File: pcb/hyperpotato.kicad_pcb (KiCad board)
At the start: 2 copper layers, 116.5 x 93.7 mm, 37 parts, among them J1 Conn_01x02_Socket, J2 Conn_01x03_Pin, Q1 AO3401A, SW1 SW_Push_45deg, SW10 SW_Push_45deg, SW11 SW_Push_45deg, SW12 SW_Push_45deg, SW13 SW_Push_45deg, SW14 SW_SPDT, SW15 SW_Push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

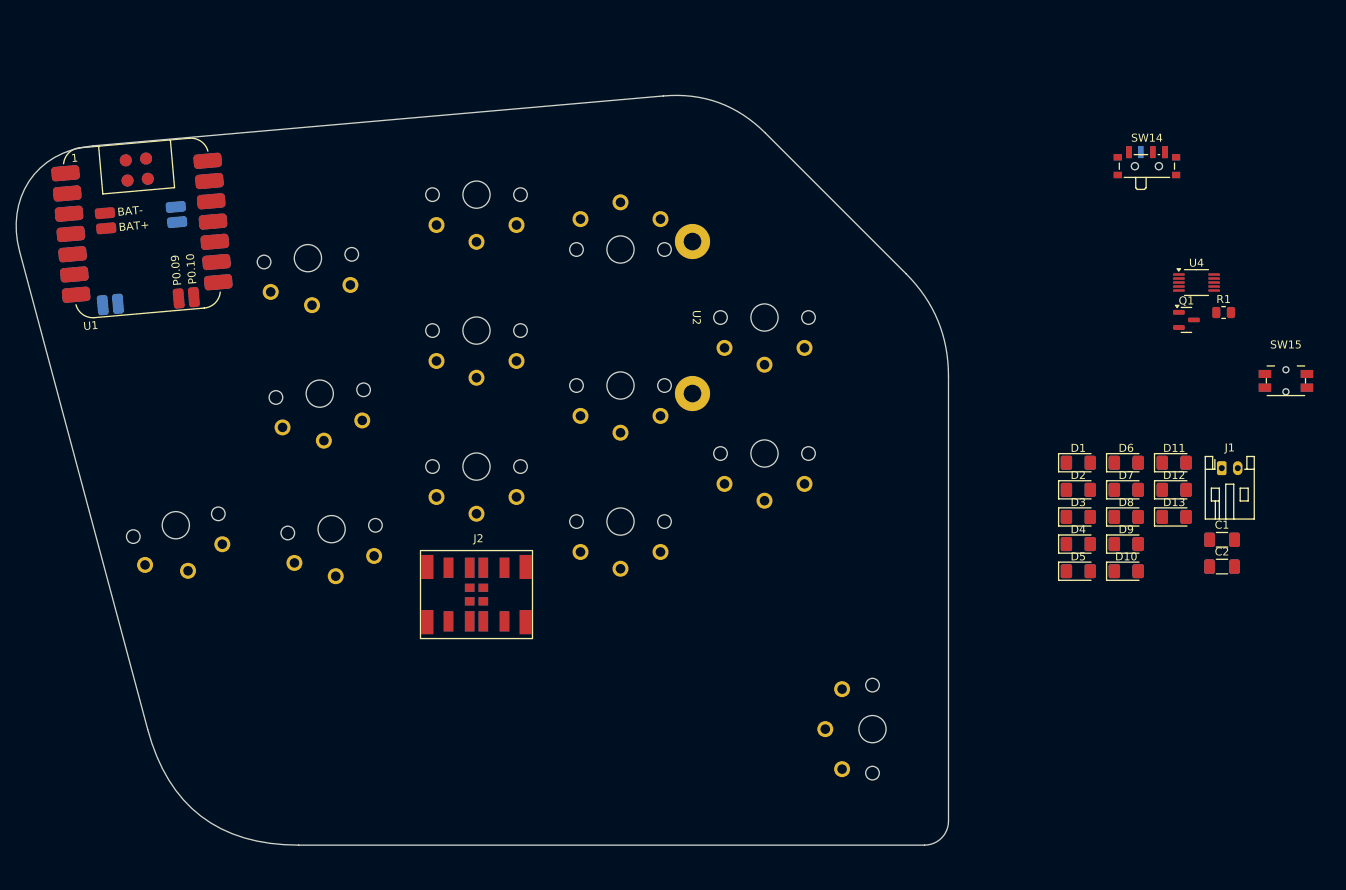
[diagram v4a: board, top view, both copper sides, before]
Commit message: Place diodes
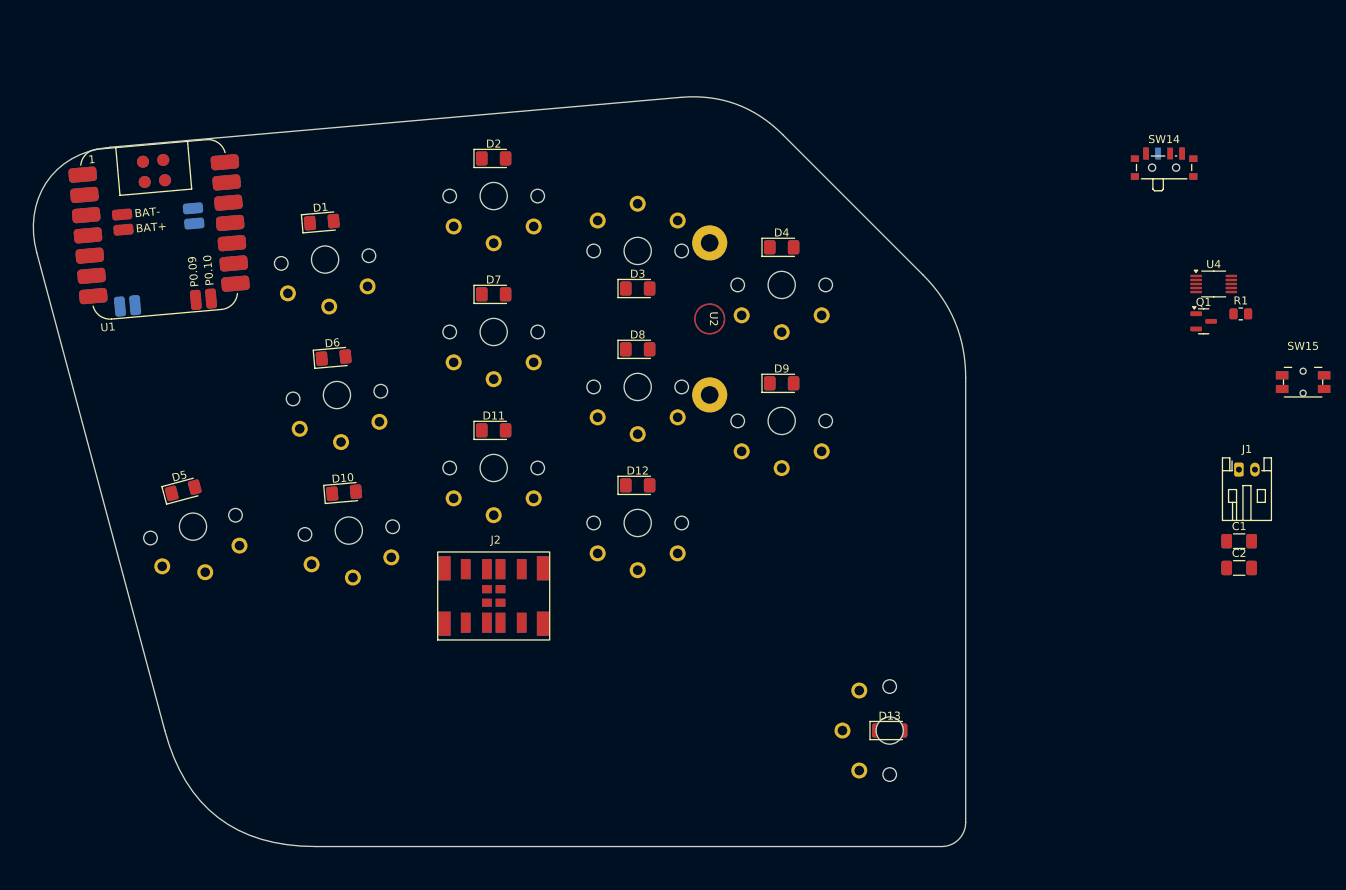
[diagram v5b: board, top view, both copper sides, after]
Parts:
- moved D5 112.3 mm to (59.0, 102.2), turned to 15 degrees
- moved D6 99.9 mm to (77.8, 85.6), turned to 5 degrees
- moved D1 99.2 mm to (76.3, 68.7), turned to 5 degrees
- moved D10 98.3 mm to (79.1, 102.5), turned to 5 degrees
- moved D11 85.2 mm to (97.8, 94.7)
- moved D2 84.0 mm to (97.8, 60.7)
- moved D7 82.8 mm to (97.8, 77.7)
- moved D12 67.1 mm to (115.8, 101.6)
- moved D8 64.6 mm to (115.8, 84.6)
- moved D3 62.0 mm to (115.8, 77.0)
- moved D4 52.4 mm to (133.8, 71.8)
- moved D9 47.5 mm to (133.8, 88.8)
- moved D13 44.5 mm to (147.3, 132.2)
- moved SW9 4.61 mm to (133.8, 93.5)
- moved SW4 4.61 mm to (133.8, 76.5)
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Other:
- board text added: "Trackpoint is going to be mounted on the right side, and the switch pin won't collide with it in this orientation. Will need to cut stab pins though."
- board text removed: "Trackpoint is going to be mounted on the right side, and the switch pin won't collide with it in this orientation. Will need to cut stab pin though."

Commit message: Re-arrange diodes
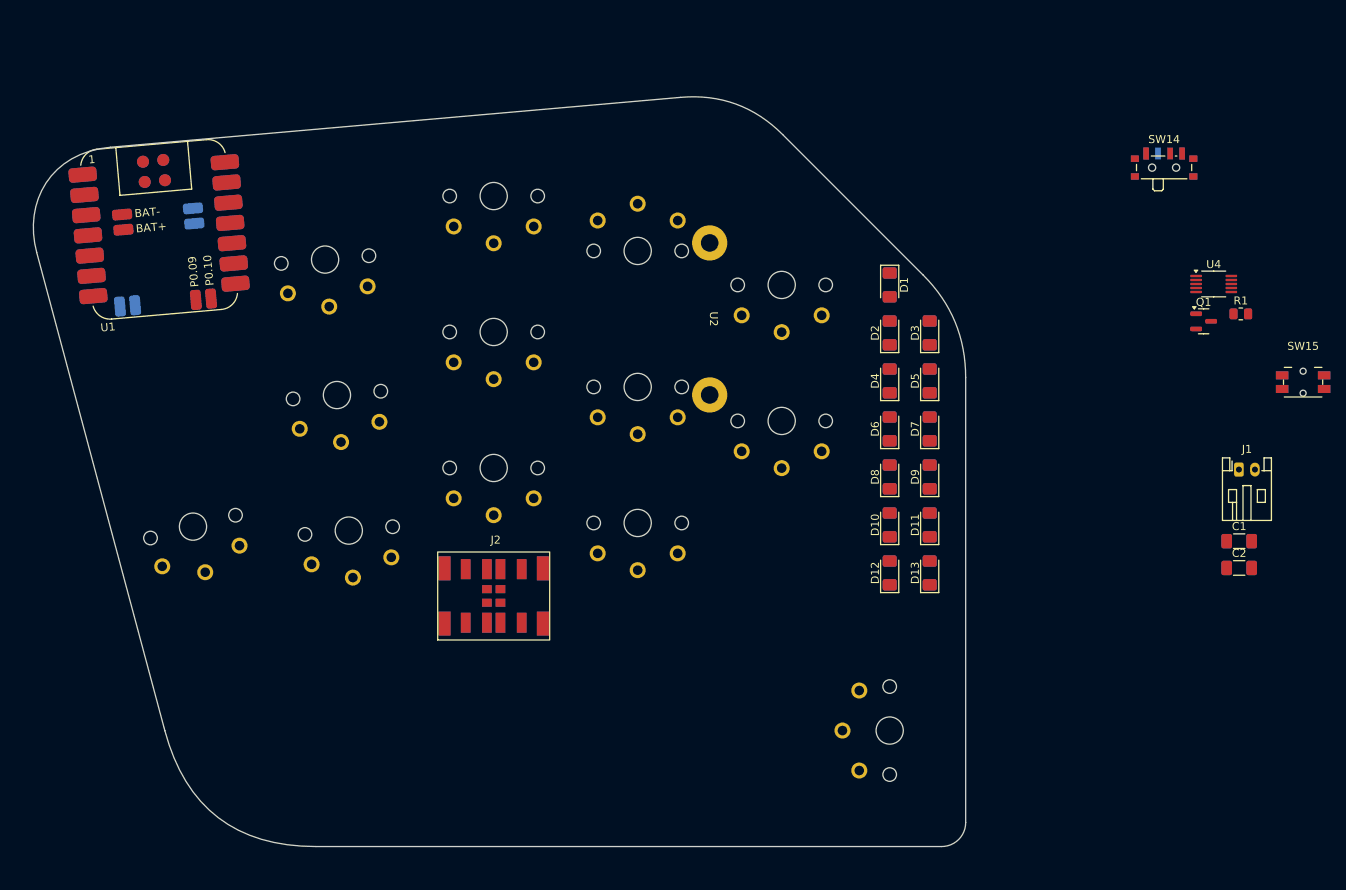
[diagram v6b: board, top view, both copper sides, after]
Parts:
- moved D5 94.3 mm to (152.3, 88.5), turned to 90 degrees
- moved D1 71.4 mm to (147.3, 76.5), turned to -90 degrees
- moved D6 70.1 mm to (147.3, 94.5), turned to 90 degrees
- moved D10 68.3 mm to (147.3, 106.5), turned to 90 degrees
- moved D7 57.0 mm to (152.3, 94.5), turned to 90 degrees
- moved D11 55.8 mm to (152.3, 106.5), turned to 90 degrees
- moved D2 54.1 mm to (147.3, 82.5), turned to 90 degrees
- moved D3 36.9 mm to (152.3, 82.5), turned to 90 degrees
- moved D8 35.3 mm to (147.3, 100.5), turned to 90 degrees
- moved D12 33.3 mm to (147.3, 112.5), turned to 90 degrees
- moved D9 21.9 mm to (152.3, 100.5), turned to 90 degrees
- moved D4 21.5 mm to (147.3, 88.5), turned to 90 degrees
- moved D13 20.3 mm to (152.3, 112.5), turned to 90 degrees
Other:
- board text added: "A few reasons to place diodes like this: - Aesthetics - The trackpoint sensor PCB would collide with them when placed in a LED hole - They are easy to solder with a hot plate this way"

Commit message: Pre-expirement changes
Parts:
- moved Q1 1.63 mm to (185.8, 82.5)

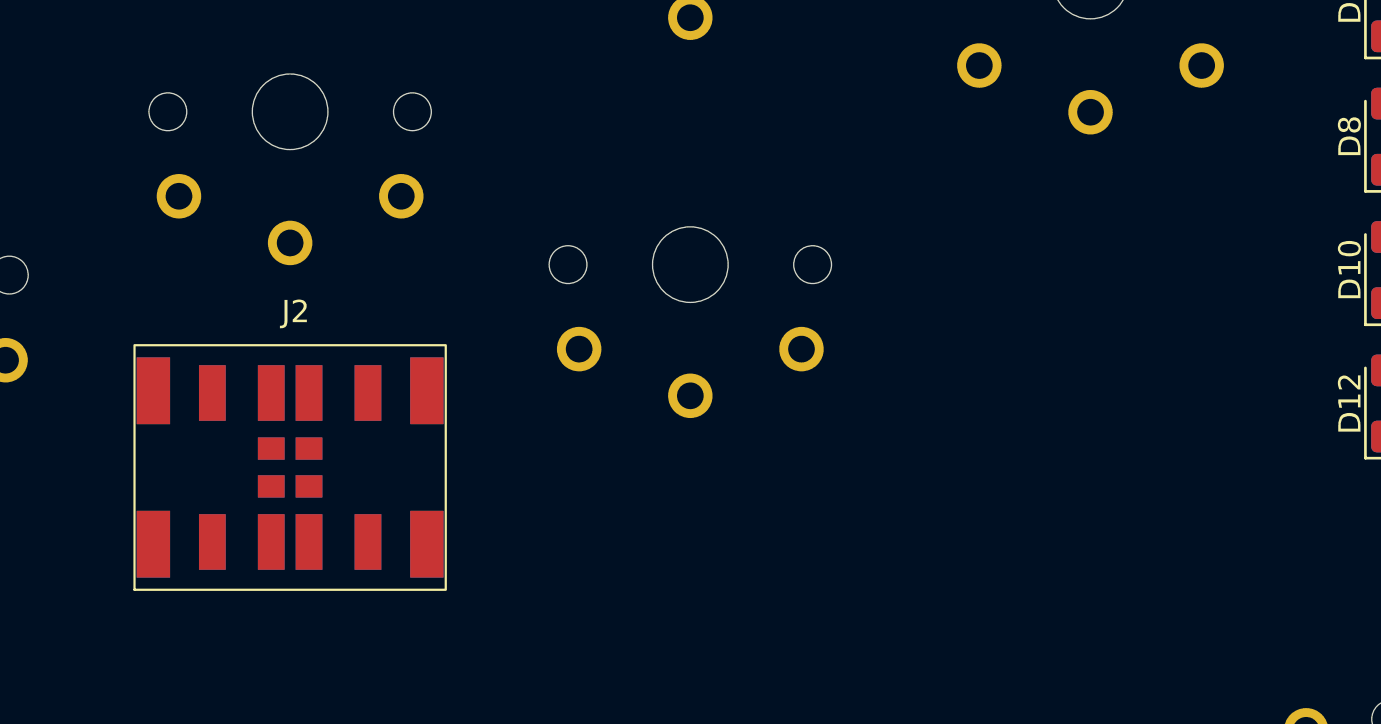
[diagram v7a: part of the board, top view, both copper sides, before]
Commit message: Relocate haptic motor
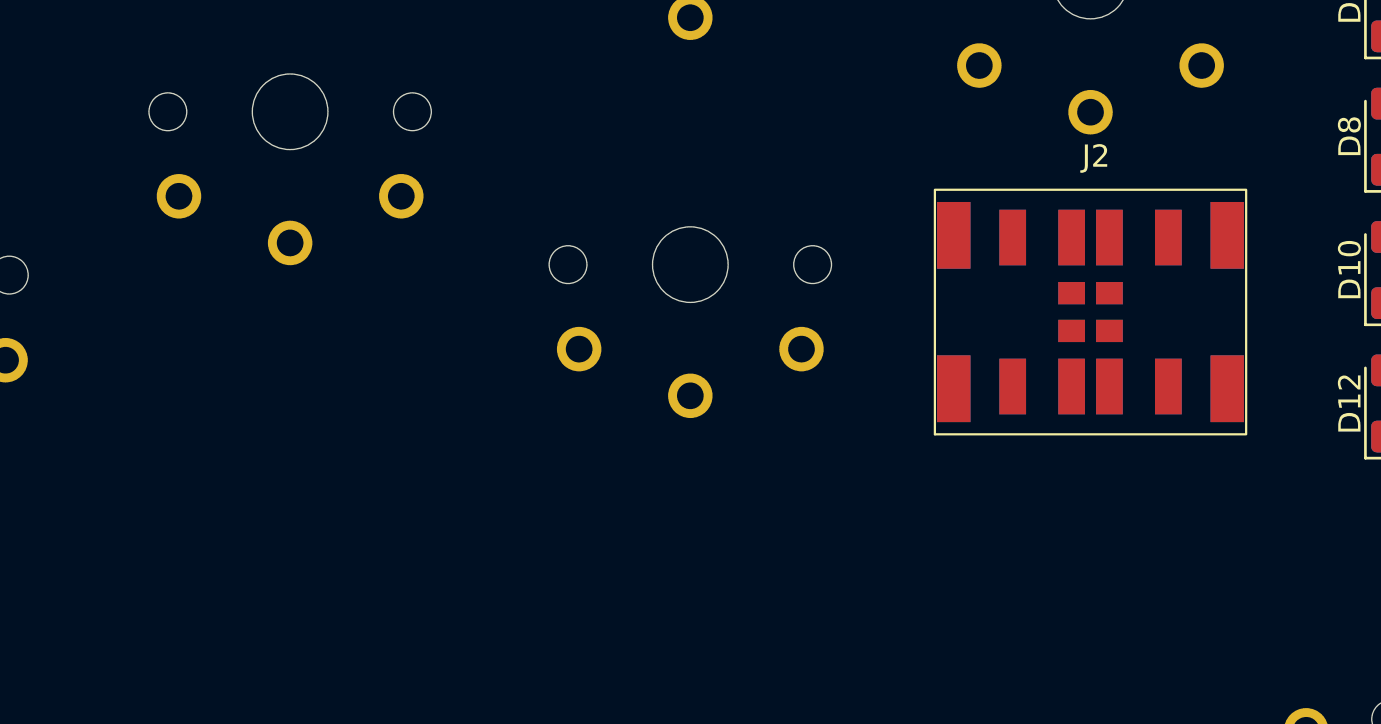
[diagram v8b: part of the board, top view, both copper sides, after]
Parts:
- moved J2 36.7 mm to (133.8, 108.4)
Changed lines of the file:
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@@
 		(pad_to_mask_clearance 0)
 		(allow_soldermask_bridges_in_footprints no)
-		(grid_origin 133.77141 76.518055)
+		(grid_origin 133.77141 93.518057)
 		(pcbplotparams
 			(layerselection 0x00010fc_ffffffff)
@@
 	(footprint "ssbb_parts:ELV1411A_reversible"
 		(layer "F.Cu")
-		(at 97.771409 115.398055)
+		(at 133.77141 108.405557)
 		(property "Reference" "J2"
 			(at 0.25 -7 0)
